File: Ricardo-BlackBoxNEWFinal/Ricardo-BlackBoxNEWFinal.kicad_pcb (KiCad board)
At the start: 4 copper layers, 62 x 33 mm, 82 parts, among them IC1 XTSD08GLGEAG, J1 RBUS, J2 USB_C_Receptacle_USB2.0, U1 ESP32-S3, U2 SN65HVD230, U3 LM66200DRLR, U4 MAX77827AEFD+T, U5 SC4215, Y1 40MHz±10ppm

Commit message: RicardoBlackBox_20_08_2023(3)
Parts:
- moved TP3 9.62 mm to (170.6, 61.8)
- moved TP11 9.04 mm to (168.7, 53.0)
- moved C15 0.21 mm to (140.8, 58.0)
- moved C16 0.17 mm to (141.9, 58.0)
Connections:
- U1 pad 40: /MISO -> /MOSI
- U1 pad 41: /MOSI -> /MISO
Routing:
- net /MOSI: track 26.1 -> 14.9 mm
- net /MISO: track 15.3 -> 14.6 mm
- net GND: vias 47 -> 46

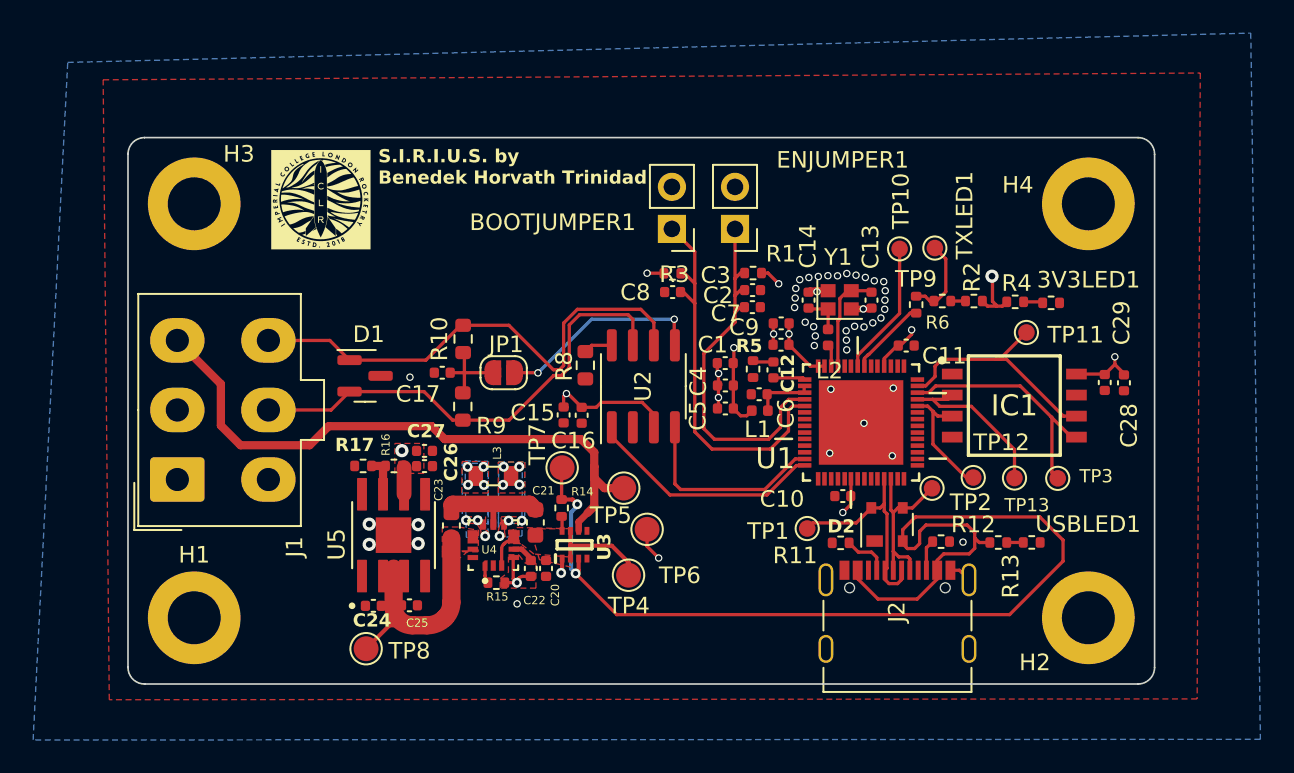
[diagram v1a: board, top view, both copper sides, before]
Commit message: RicardoBlackBox_21_08_2023
Changed some silkscreens and removed some disconnected tracks
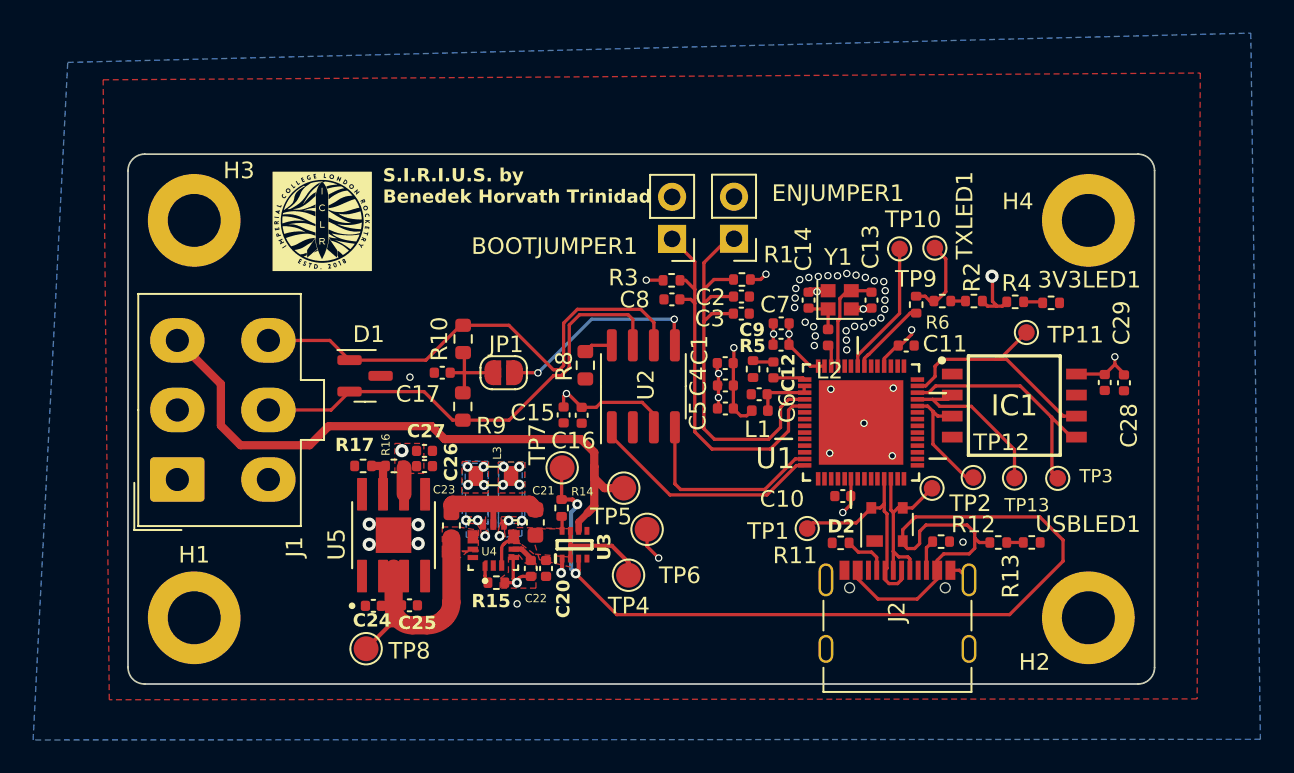
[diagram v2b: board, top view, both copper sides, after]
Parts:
- moved G*** 1.31 mm to (126.2, 46.3)
- moved H3 1.00 mm to (118.5, 46.2)
- moved H4 1.00 mm to (172.5, 46.2)
- moved C3 0.78 mm to (151.5, 51.9)
- moved C2 0.78 mm to (151.5, 50.8)
- moved R1 0.78 mm to (151.6, 49.8)
- moved BOOTJUMPER1 0.60 mm to (147.3, 47.3)
- moved ENJUMPER1 0.60 mm to (151.1, 47.3)
- moved C8 0.44 mm to (147.3, 51.0)
- moved R3 0.42 mm to (147.3, 49.8)
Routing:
- net /CHIP_PU: track 23.0 -> 26.5 mm
- net /BOOT: track 23.9 -> 23.2 mm
- net +3V3: track 35.8 -> 35.3 mm
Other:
- board size 62 x 33 mm -> 62 x 32 mm

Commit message: ordering
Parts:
- 3V3LED1: value 3V3LED -> BLUE_LED
- C12: value 4.2pF -> DNP
- R5: value 47.5 -> DNP
- TXLED1: value TX_LED -> GREEN_LED
- U1: footprint iclr:QFN40P700X700X90-57N -> ICLR:QFN40P700X700X90-57N
- moved TP2 0.81 mm to (163.4, 63.1)
- moved C28 0.54 mm to (174.1, 56.0)
- moved C29 0.35 mm to (173.1, 56.0)
- moved C7 0.29 mm to (153.9, 52.7)
- moved C10 0.19 mm to (157.6, 63.1)
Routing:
- net GND: track 30.8 -> 17.4 mm, vias 46 -> 108
- net +3V3: track 35.3 -> 34.4 mm, vias 11 -> 13
- added copper zone on In2.Cu, net +3V3
- added copper zone on In1.Cu, net GND
- removed copper zone on In1.Cu, net +3V3
